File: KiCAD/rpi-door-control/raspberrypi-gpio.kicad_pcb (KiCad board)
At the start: 2 copper layers, 85 x 56 mm, 1 part, among them P1 CONN_13X2

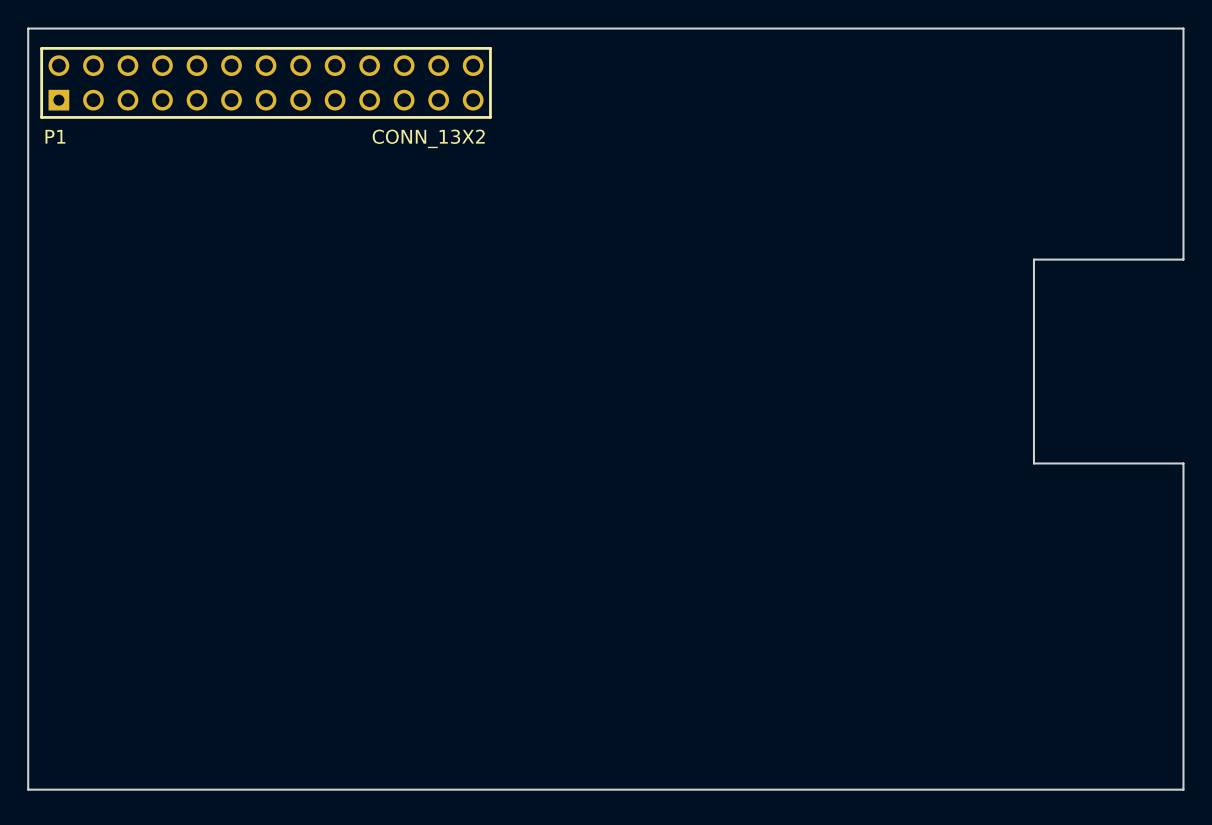
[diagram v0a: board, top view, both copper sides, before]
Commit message: Added terminal block footprint and initial layout of board connectors
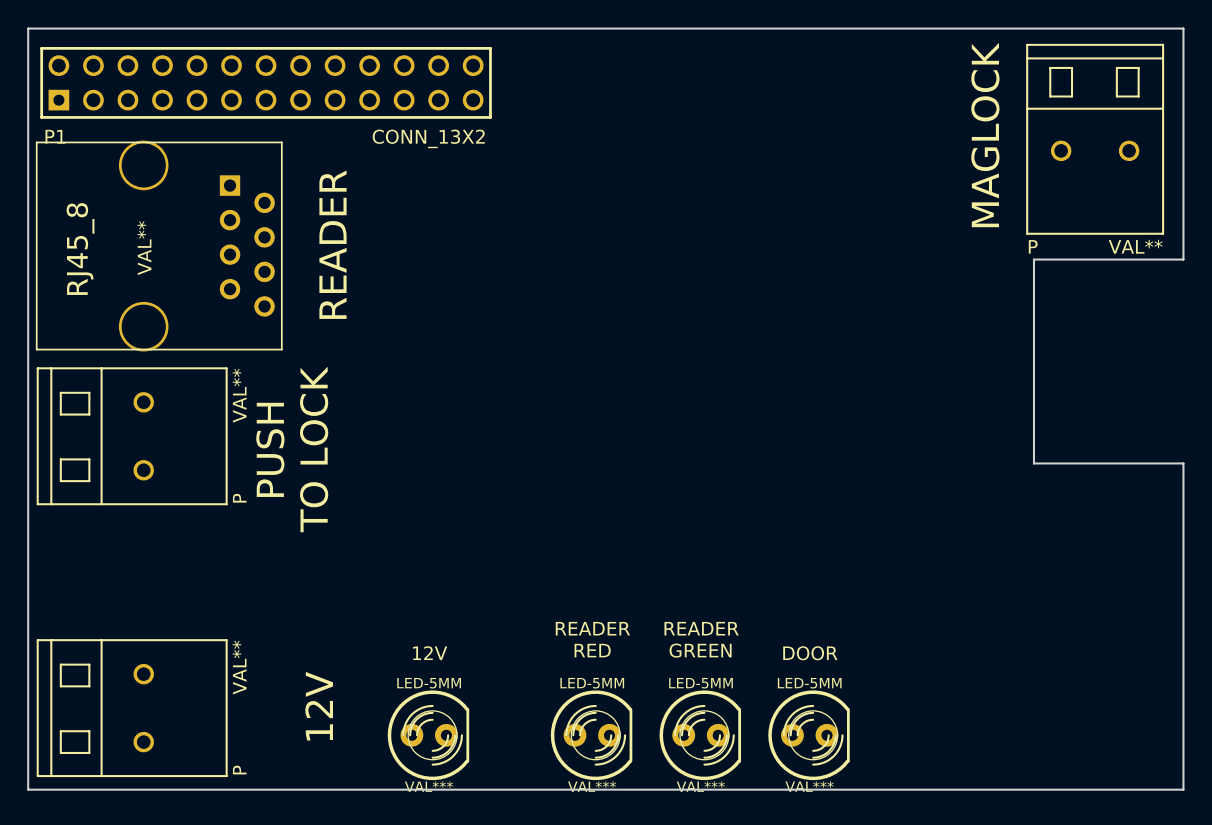
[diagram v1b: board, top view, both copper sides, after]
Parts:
- added LED-5MM: VAL***, LED-5MM, F.Cu at (193.0, 177.0)
- added LED-5MM: VAL***, LED-5MM, F.Cu at (185.0, 177.0)
- added LED-5MM: VAL***, LED-5MM, F.Cu at (201.0, 177.0)
- added LED-5MM: VAL***, LED-5MM, F.Cu at (173.0, 177.0)
- added P: VAL**, 2Pole_Terminal_block, F.Cu at (222.0, 134.0)
- added P: VAL**, 2Pole_Terminal_block, F.Cu at (152.0, 155.0)
- added P: VAL**, 2Pole_Terminal_block, F.Cu at (152.0, 175.0)
- added RJ45_8: VAL**, RJ45_8, F.Cu at (152.0, 141.0)
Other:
- board text added: "12V"
- board text added: "DOOR"
- board text added: "MAG LOCK"
- board text added: "MAGLOCK"
- board text added: "PUSH TO LOCK"
- board text added: "READER"
- board text added: "READER GREEN"
- board text added: "READER RED"

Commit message: components placed - who knows if the layout is any good or not
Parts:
- removed LED-5MM (x4): VAL***, LED-5MM
- removed P (x3): VAL**, 2Pole_Terminal_block
- removed RJ45_8: VAL**, RJ45_8
- added D1: LED, LED-3MM, F.Cu at (193.0, 176.0)
- added D2: LED, LED-3MM, F.Cu at (185.0, 176.0)
- added D3: LED, LED-3MM, F.Cu at (201.0, 176.0)
- added D4: LED, LED-3MM, F.Cu at (172.0, 176.0)
- added D5: 1N4007, DO-41, F.Cu at (198.0, 133.0)
- added J1: RJ45, RJ45_8, F.Cu at (153.0, 142.0)
- added P2: CONN_2, C2_KF103, F.Cu at (153.0, 156.0)
- added P3: CONN_2, C2_KF103, F.Cu at (222.0, 134.0)
- added P4: CONN_2, C2_KF103, F.Cu at (153.0, 174.0)
- added Q1: N3904, TO92, F.Cu at (184.0, 163.0)
- added R1: 10K, R5, F.Cu at (220.0, 160.0)
- added R2: 1.8K, R5, F.Cu at (198.0, 160.0)
- added R3: 3.3K, R5, F.Cu at (198.0, 165.0)
- added R4: 330, R5, F.Cu at (175.0, 142.0)
- added R5: 330, R5, F.Cu at (171.0, 142.0)
- added R6: 330, R5, F.Cu at (179.0, 142.0)
- added R7: 1K, R5, F.Cu at (188.0, 148.0)
- added R8: 2K, R5, F.Cu at (153.0, 165.0)
- added SW1: SW_PUSH, SW_PUSH_SMALL, F.Cu at (174.0, 156.0)
- added U1: RELAY, RELAY_AZ942, F.Cu at (210.0, 149.0)
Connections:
- P1 pad 10: (no net) -> /RXD
- P1 pad 11: (no net) -> /GPIO17
- P1 pad 13: (no net) -> /BELL
- P1 pad 16: (no net) -> /GPIO23
- P1 pad 18: (no net) -> /GPIO24
- P1 pad 22: (no net) -> /GPIO25

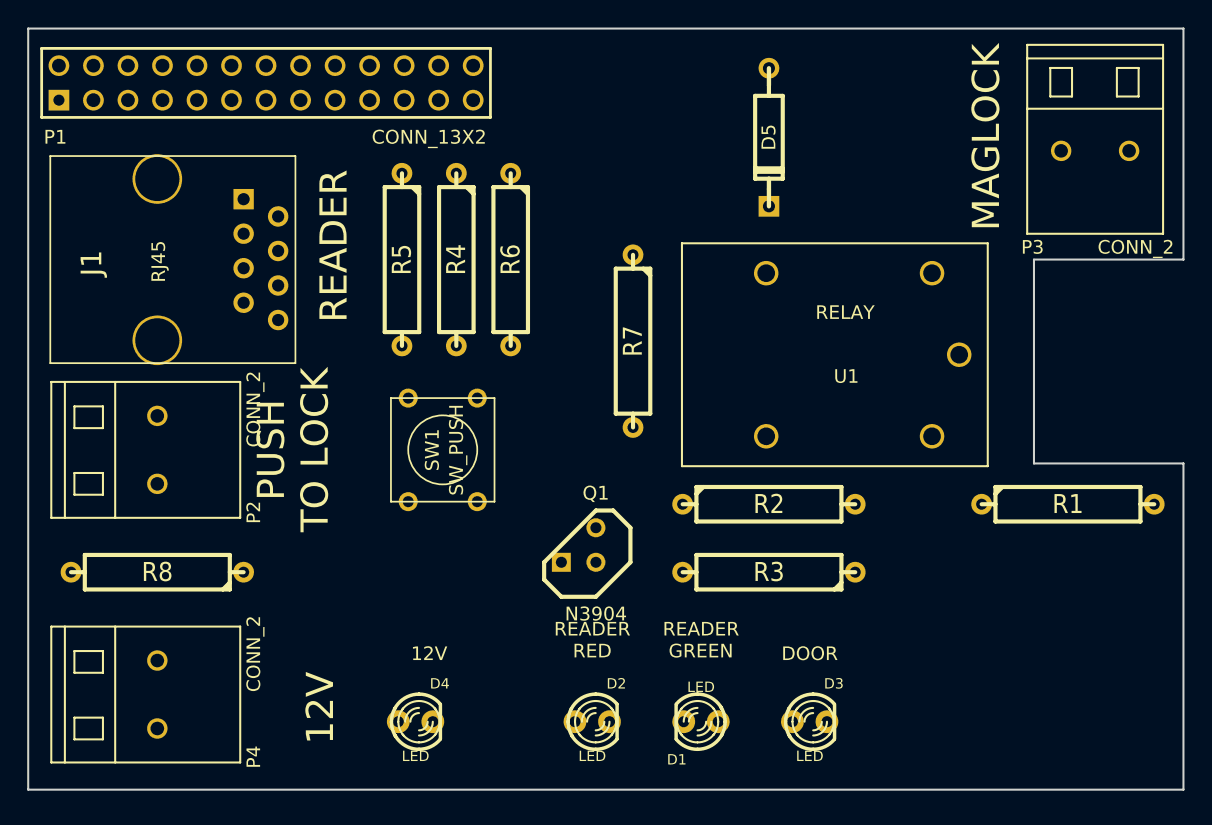
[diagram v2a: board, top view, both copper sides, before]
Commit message: Added autorouter files and generated single layer routes
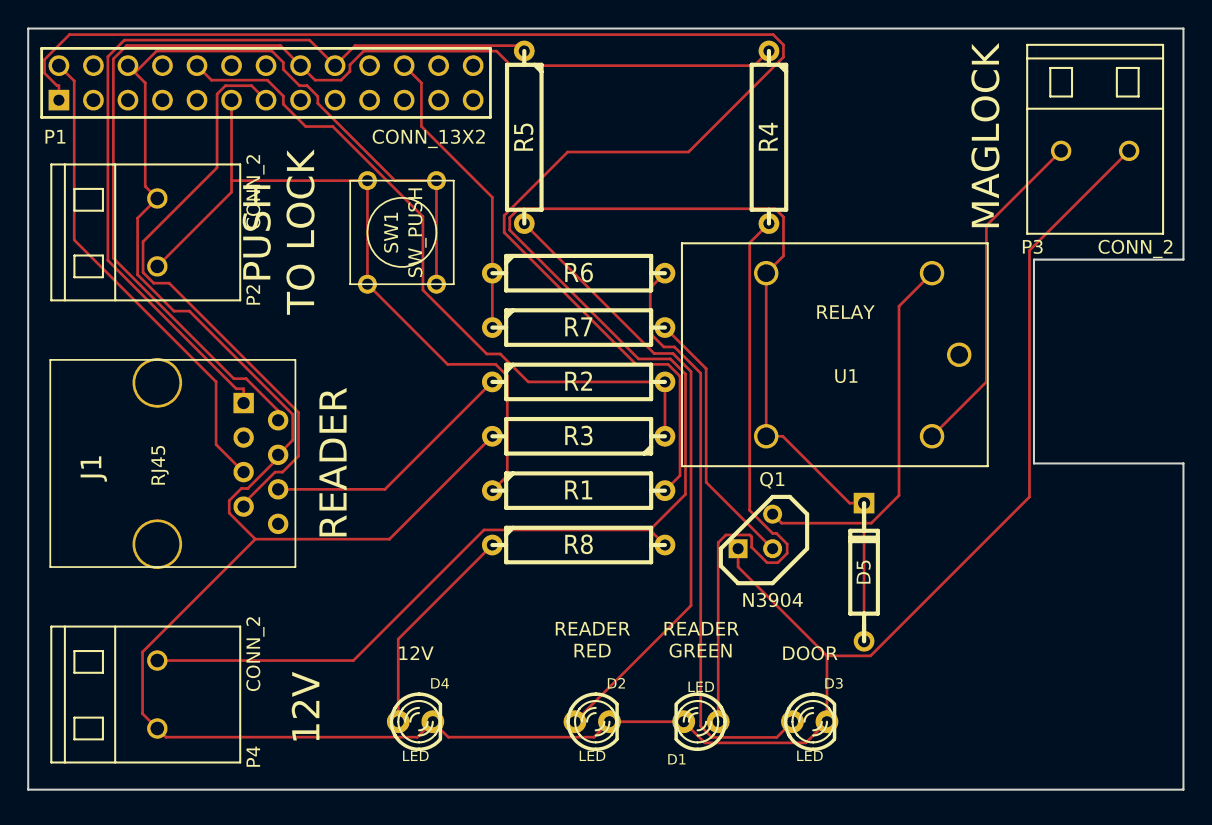
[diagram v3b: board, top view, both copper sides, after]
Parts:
- moved R1 36.0 mm to (184.0, 159.0)
- moved D5 32.8 mm to (205.0, 165.0), turned to 90 degrees
- moved R8 31.1 mm to (184.0, 163.0), turned to 0 degrees
- moved R4 24.7 mm to (198.0, 133.0)
- moved R3 17.2 mm to (184.0, 155.0)
- moved R2 16.6 mm to (184.0, 151.0)
- moved SW1 16.3 mm to (171.0, 140.0)
- moved P2 16.0 mm to (153.0, 140.0)
- moved J1 15.0 mm to (153.0, 157.0)
- moved Q1 13.0 mm to (197.0, 162.0)
- moved R5 12.7 mm to (180.0, 133.0)
- moved R6 5.10 mm to (184.0, 143.0), turned to 0 degrees
- moved R7 4.12 mm to (184.0, 147.0), turned to 0 degrees
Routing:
- net GND: track 0.00 -> 234.1 mm
- net +12V: track 0.00 -> 119.1 mm
- net +3.3V: track 0.00 -> 112.7 mm
- net /GPIO23: track 0.00 -> 83.9 mm
- net /GPIO24: track 0.00 -> 62.6 mm
- net /GPIO17: track 0.00 -> 54.1 mm
- net /RXD: track 0.00 -> 51.6 mm
- net N-0000023: track 0.00 -> 46.2 mm
- net N-0000024: track 0.00 -> 46.1 mm
- net /BELL: track 0.00 -> 44.3 mm
- net N-0000025: track 0.00 -> 43.3 mm
- net N-0000017: track 0.00 -> 36.5 mm
- net +5V: track 0.00 -> 35.5 mm
- net N-000001: track 0.00 -> 24.9 mm
- net /GPIO25: track 0.00 -> 22.0 mm
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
